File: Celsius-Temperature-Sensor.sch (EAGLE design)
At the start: 18 parts, among them Q1 BSS138, Q2 BSS138

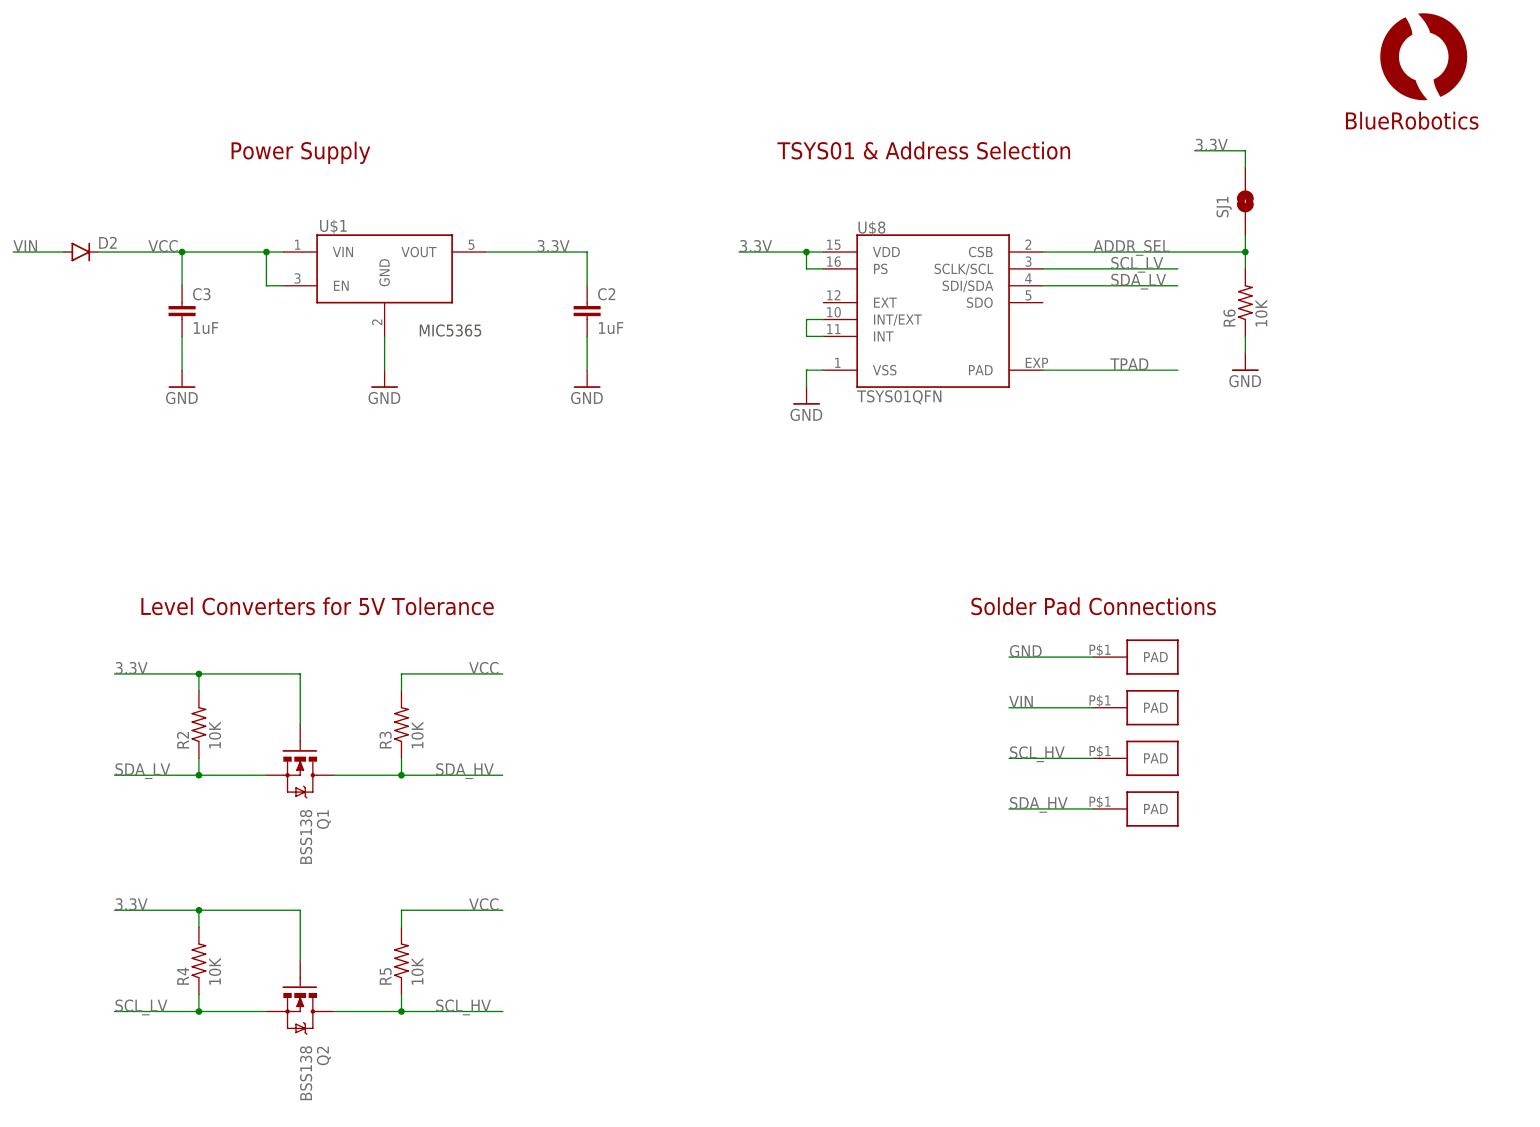
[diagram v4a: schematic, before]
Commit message: Removed diode because it caused a large enough Vf to drop voltage outside of range needed to achieve high accuracy Acc1. Also added a few ground vias. Ordering production version from this revision.
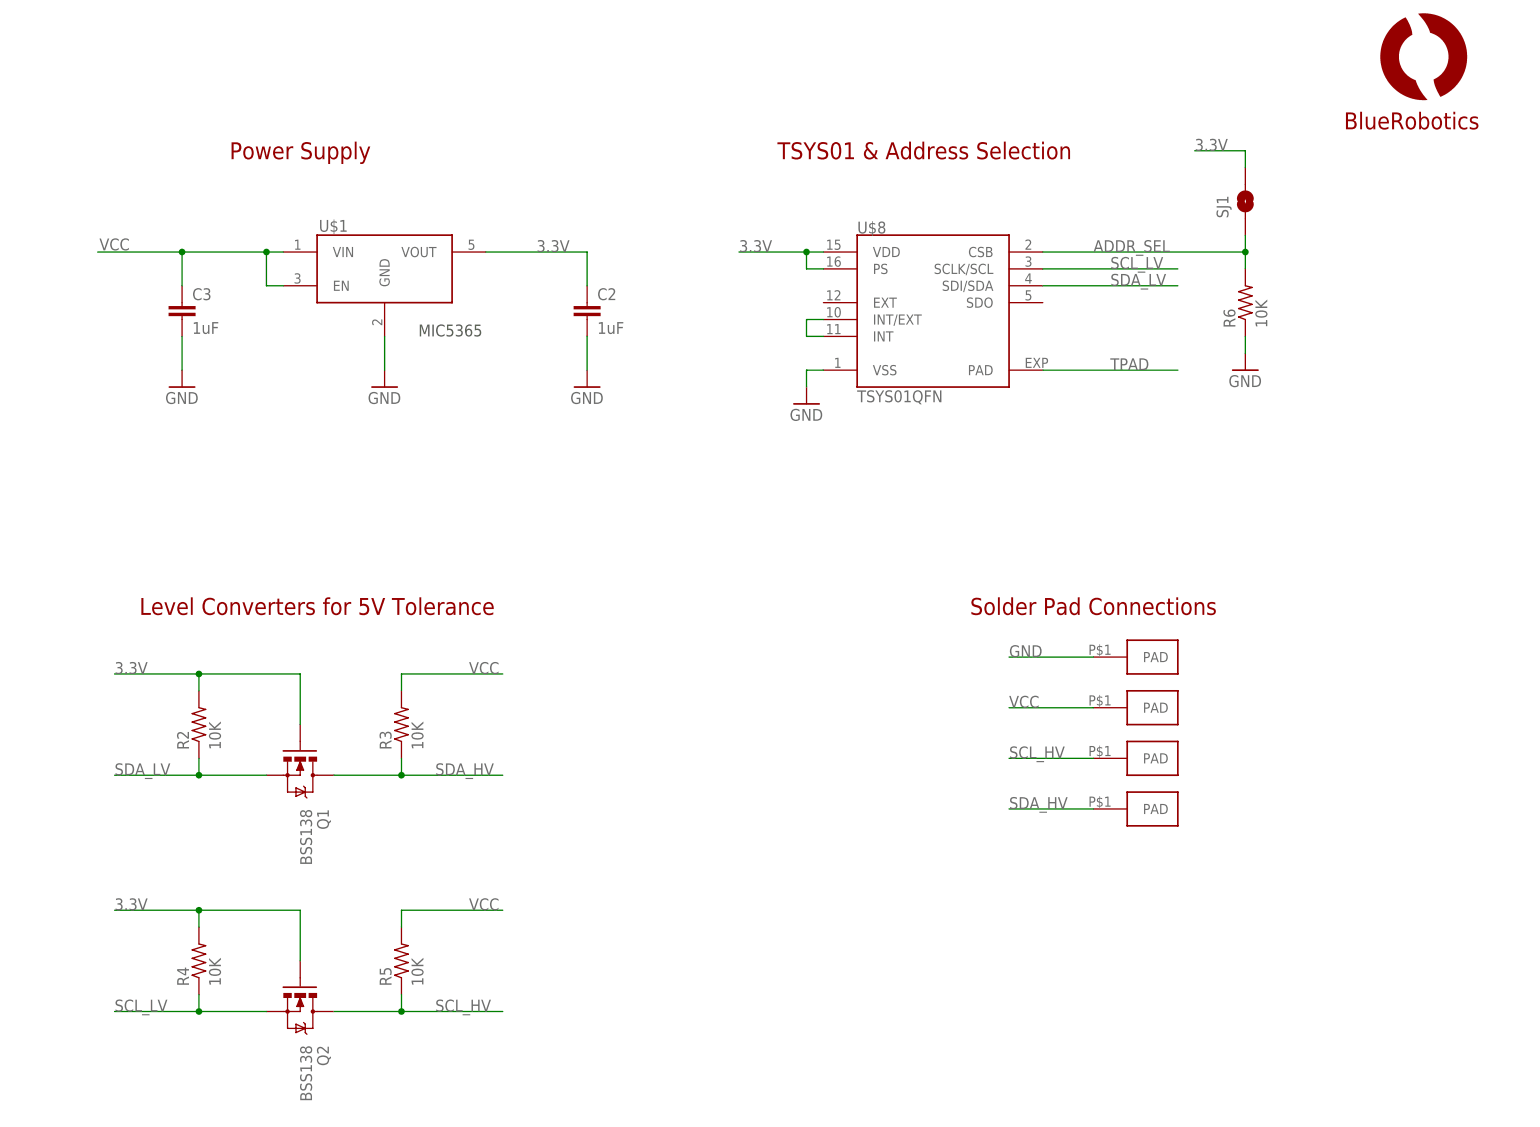
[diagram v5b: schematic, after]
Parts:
- removed D2: (no value), SparkFun-DiscreteSemi:DIODESOD523
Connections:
- removed net VIN: D2.A, U$4.PAD
- net VCC: now also U$4.PAD; no longer D2.C
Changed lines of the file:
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@@
 <part name="GND5" library="supply1" deviceset="GND" device=""/>
 <part name="GND6" library="supply1" deviceset="GND" device=""/>
-<part name="D2" library="SparkFun-DiscreteSemi" deviceset="DIODE" device="SOD523"/>
 <part name="U$1" library="BlueRobotics-Main" deviceset="VREG-MIC5365" device=""/>
 <part name="C3" library="resistor" deviceset="C-EU" device="C0402" value="1uF"/>
@@
 <instance part="GND5" gate="1" x="-22.86" y="35.56"/>
 <instance part="GND6" gate="1" x="7.62" y="35.56"/>
-<instance part="D2" gate="G$1" x="-68.58" y="55.88"/>
 <instance part="U$1" gate="G$1" x="-33.02" y="50.8"/>
 <instance part="C3" gate="G$1" x="-53.34" y="48.26"/>
@@
 <segment>
 <wire x1="-38.1" y1="55.88" x2="-40.64" y2="55.88" width="0.1524" layer="91"/>
-<label x="-58.42" y="55.88" size="1.778" layer="95"/>
-<pinref part="D2" gate="G$1" pin="C"/>
+<label x="-65.786" y="56.134" size="1.778" layer="95"/>
 <pinref part="U$1" gate="G$1" pin="VIN"/>
 <pinref part="U$1" gate="G$1" pin="EN"/>
@@
 <junction x="-53.34" y="55.88"/>
 </segment>
+<segment>
+<wire x1="83.82" y1="-12.7" x2="71.12" y2="-12.7" width="0.1524" layer="91"/>
+<label x="71.12" y="-12.7" size="1.778" layer="95"/>
+<pinref part="U$4" gate="G$1" pin="PAD"/>
+</segment>
 </net>
 <net name="SCL_HV" class="0">
@@
 </segment>
 </net>
-<net name="VIN" class="0">
-<segment>
-<wire x1="83.82" y1="-12.7" x2="71.12" y2="-12.7" width="0.1524" layer="91"/>
-<label x="71.12" y="-12.7" size="1.778" layer="95"/>
-<pinref part="U$4" gate="G$1" pin="PAD"/>
-</segment>
-<segment>
-<pinref part="D2" gate="G$1" pin="A"/>
-<wire x1="-71.12" y1="55.88" x2="-78.74" y2="55.88" width="0.1524" layer="91"/>
-<label x="-78.74" y="55.88" size="1.778" layer="95"/>
-</segment>
-</net>

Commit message: Added PDF schematic, updated readme.
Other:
- note added: "Pull-down sets default address to 0x77"
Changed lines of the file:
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@@
 <text x="-35.56" y="71.12" size="2.54" layer="94" align="center">Power Supply</text>
 <text x="-17.78" y="43.18" size="1.778" layer="97">MIC5365</text>
+<text x="114.3" y="53.34" size="1.778" layer="97">Pull-down sets default
+address to 0x77</text>
 </plain>
 <instances>
@@
 </schematic>
 </drawing>
+<compatibility>
+<note version="6.3" minversion="6.2.2" severity="warning">
+Since Version 6.2.2 text objects can contain more than one line,
+which will not be processed correctly with this version.
+</note>
+</compatibility>
 </eagle>

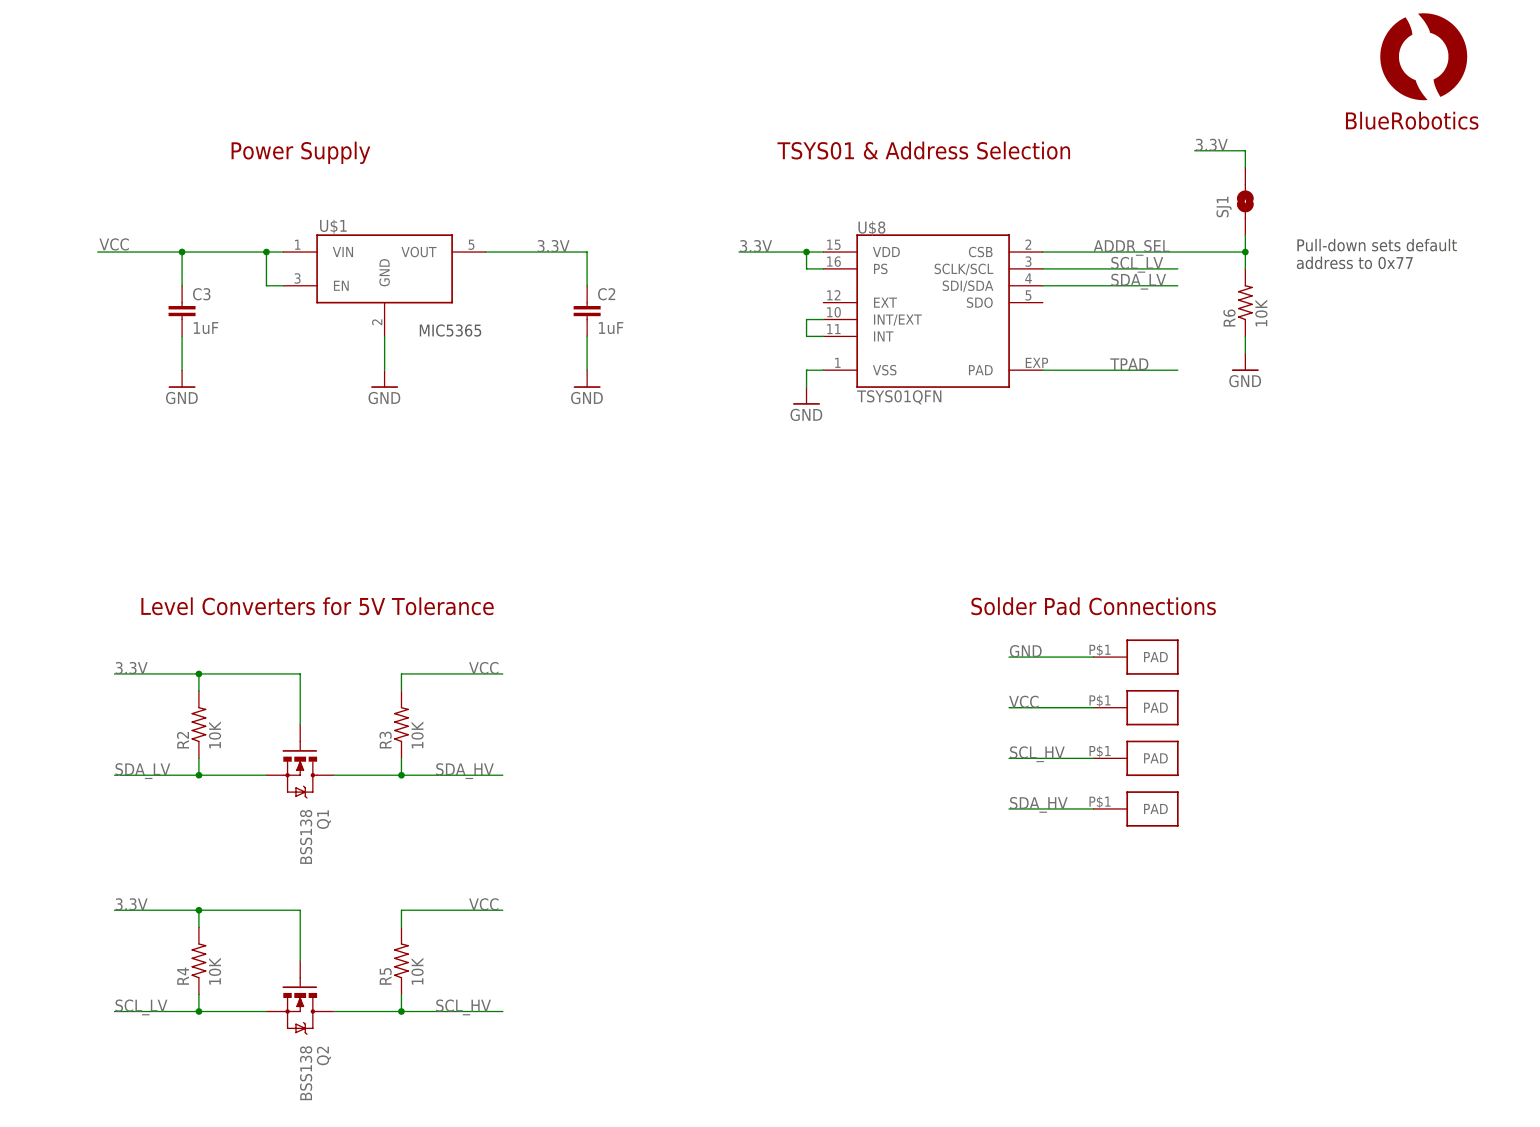
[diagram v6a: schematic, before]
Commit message: Fixed for compatibility with DroneCode autopilots.
Removed logic level converters.
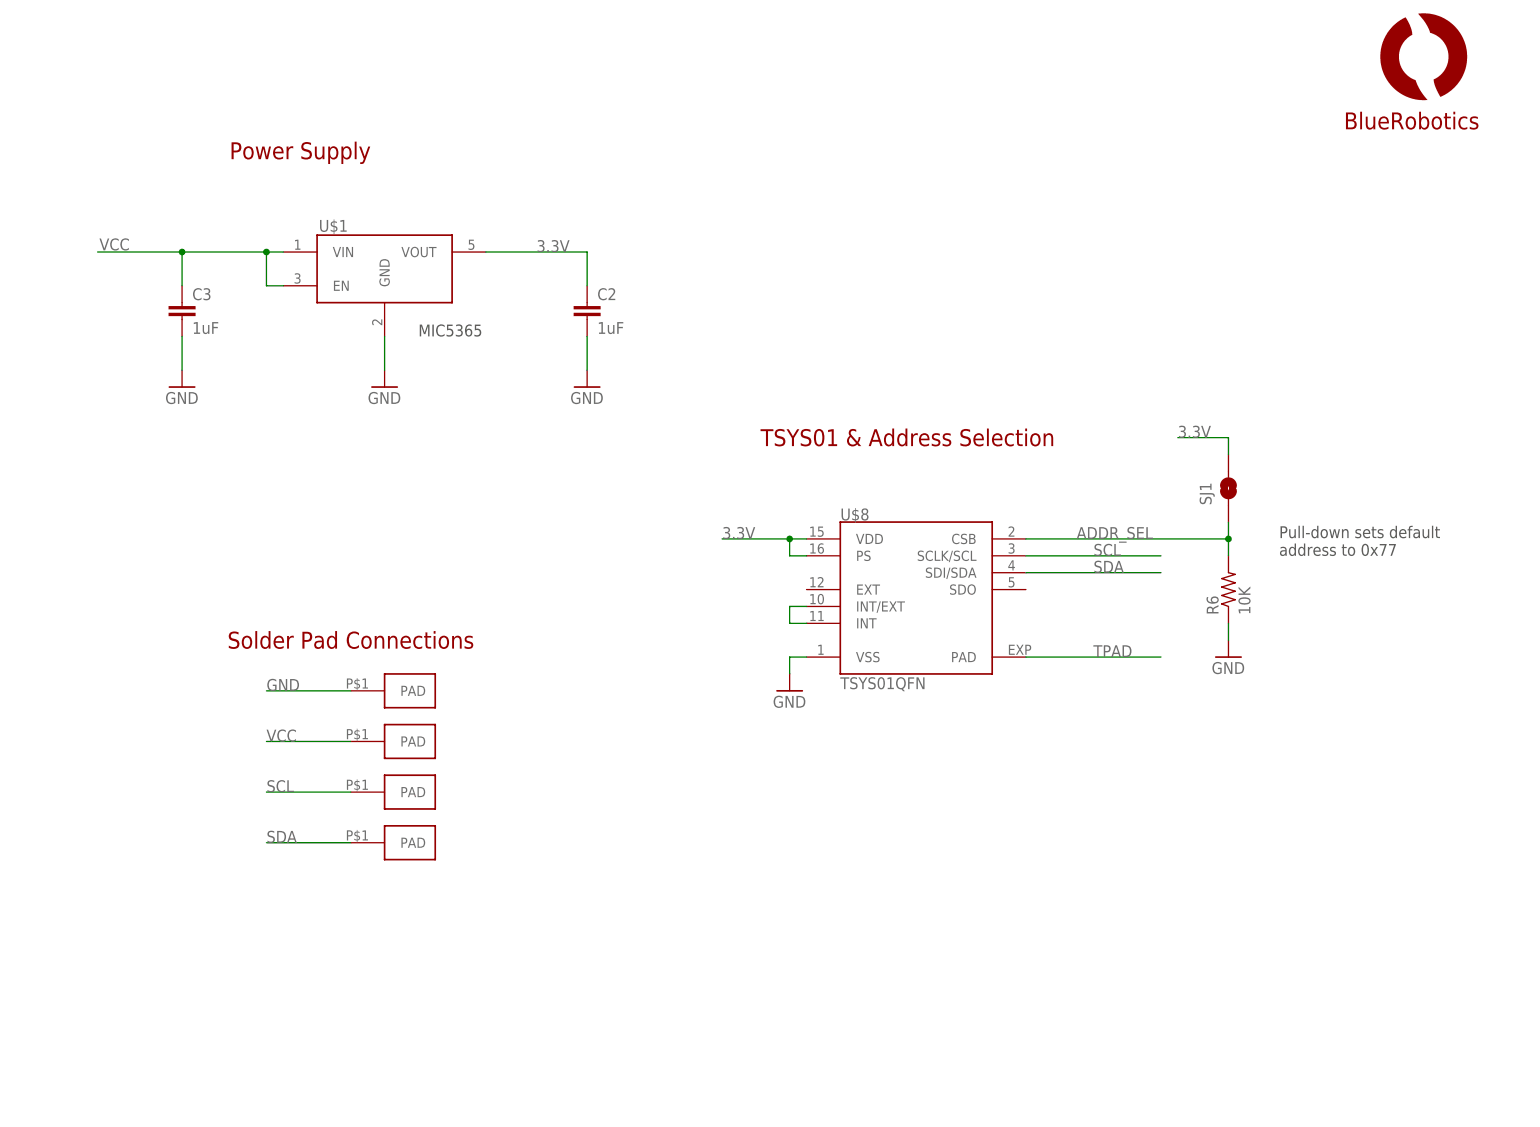
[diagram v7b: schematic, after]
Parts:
- removed Q1, Q2: BSS138, SparkFun-DiscreteSemi:MOSFET-NCHANNEL2N7002PW
- removed R2, R3, R4, R5: 10K, resistor:R-US_R0402
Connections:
- removed net SCL_HV: Q2.D, R5.1, U$5.PAD
- removed net SCL_LV: Q2.S, R4.1, U$8.SCLK/SCL
- removed net SDA_HV: Q1.D, R3.1, U$6.PAD
- removed net SDA_LV: Q1.S, R2.1, U$8.SDI/SDA
- new net SCL: U$5.PAD, U$8.SCLK/SCL
- new net SDA: U$6.PAD, U$8.SDI/SDA
- net 3.3V: no longer Q1.G, Q2.G, R2.2, R4.2
- net VCC: no longer R3.2, R5.2
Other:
- note removed: "Level Converters for 5V Tolerance"
- moved on the sheet: R6, SJ1, U$8
